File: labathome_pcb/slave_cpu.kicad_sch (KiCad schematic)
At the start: 49 parts, among them J1 HALL, J25 TC-2030, J27 ADDA, J28 Brushless, J34 STM32 EXT, J36 PROG_STM, U16 LM358, U3 DRV8313, U5 STM32G431R8Tx

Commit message: Optimized PCB
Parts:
- removed J25: TC-2030, Connector:Tag-Connect_TC2030-IDC-NL_2x03_P1.27mm_Vertical, symbol Connector:Conn_ARM_SWD_TagConnect_TC2030-NL

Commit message: Bus servos
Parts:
- removed C10, C8, C9: 10p, Capacitor_SMD:C_0402_1005Metric, symbol Device:C
- removed C38: 10n/35V, Capacitor_SMD:C_0402_1005Metric, symbol Device:C
- removed C39: 100u, Capacitor_SMD:CP_Elec_6.3x5.4, symbol Device:C_Polarized
- removed C51: u1/16V, Capacitor_SMD:C_0603_1608Metric, symbol Device:C
- removed C52, C63: u1/35V, Capacitor_SMD:C_0603_1608Metric, symbol Device:C
- removed C61: 4u7/6V3, Capacitor_SMD:C_0402_1005Metric, symbol Device:C
- removed J1: HALL, liebler_CONN:PhoenixContact_MC_1,5_4-G-3.5_1x04_P3.50mm_Horizontal_smallerCourtyard, symbol Connector_Generic:Conn_01x04
- removed J28: Brushless, liebler_CONN:PhoenixContact_MC_1,5_4-G-3.5_1x04_P3.50mm_Horizontal_smallerCourtyard, symbol Connector_Generic:Conn_01x04
- removed R10, R14, R16: 2k2, Resistor_SMD:R_0402_1005Metric, symbol Device:R
- removed R17, R51, R63, R64: 10k, Resistor_SMD:R_0201_0603Metric, symbol Device:R
- removed R38: r1, Resistor_SMD:R_2010_5025Metric, symbol Device:R
- removed U3: DRV8313, Package_SO:HTSSOP-28-1EP_4.4x9.7mm_P0.65mm_EP2.85x5.4mm_ThermalVias, symbol liebler_SEMICONDUCTORS:DRV8313
- added R22: 1k, Resistor_SMD:R_0402_1005Metric, symbol Device:R
- J34: now not fitted
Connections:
- net PB12: no longer U5.34 (PB12)
- net UART3_RX: no longer U5.33 (PB11)
- net UART3_TX: no longer U5.30 (PB10)
- net +24V renamed 5-24V
- net ADC0 renamed ADC0_U1T
- net ADC1 renamed ADC1_U1R
- net Servo0 renamed STEPPER_DIR1
- net Servo1 renamed STEPPER_STEP1
- net Servo2 renamed STEPPER_STEP2
- net Servo3 renamed STEPPER_DIR2
- new net SERVO_BUS_TX_EN: U5.34 (PB12)
- new net STEPPER_UART: R22.2, U5.33 (PB11)
- new net U3T: R22.1, U5.30 (PB10)
- no-connect marks 1 -> 0
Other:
- note added: "T1.1, LPUART1.R"
- note added: "T1.2, LPUART1.T"
- note added: "T1.3"
- note added: "T1.4"
- note added: "T15.1, U2.T"
- note added: "T15.2, U2.R"
- note added: "T2.1"
- note added: "T2.2"
- note removed: "Brushless Driver"
- note removed: "T15.1"
- note removed: "T15.2"

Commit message: Various
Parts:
- added TP2: OP3Q, TestPoint:TestPoint_Pad_1.5x1.5mm, symbol Connector:TestPoint
- added TP3: OP3-, TestPoint:TestPoint_Pad_1.5x1.5mm, symbol Connector:TestPoint
- added TP4: OP3+, TestPoint:TestPoint_Pad_1.5x1.5mm, symbol Connector:TestPoint
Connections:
- net OPAMP3+: now also TP4.1
- net OPAMP3-: now also TP3.1
- net OPAMP3Q: now also TP2.1

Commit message: Merged
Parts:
- removed TP2: OP3Q, TestPoint:TestPoint_Pad_1.5x1.5mm, symbol Connector:TestPoint
- removed TP3: OP3-, TestPoint:TestPoint_Pad_1.5x1.5mm, symbol Connector:TestPoint
- removed TP4: OP3+, TestPoint:TestPoint_Pad_1.5x1.5mm, symbol Connector:TestPoint
- added J26: EXT, Connector_PinHeader_2.54mm:PinHeader_2x03_P2.54mm_Vertical, symbol Connector_Generic:Conn_02x03_Odd_Even
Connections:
- net SERVO_BUS_TX_EN is gone; now on net PB12: U5.34 (PB12)
- net +3V3: now also J26.1 (Pin_1)
- net GND: now also J26.6 (Pin_6)
- net OPAMP3+: now also J26.2 (Pin_2)
- net OPAMP3-: now also J26.3 (Pin_3)
- net OPAMP3Q: now also J26.5 (Pin_5)
- net PB12: now also J26.4 (Pin_4)
- net STEPPER_DIR2 renamed STEPPER_STEP3

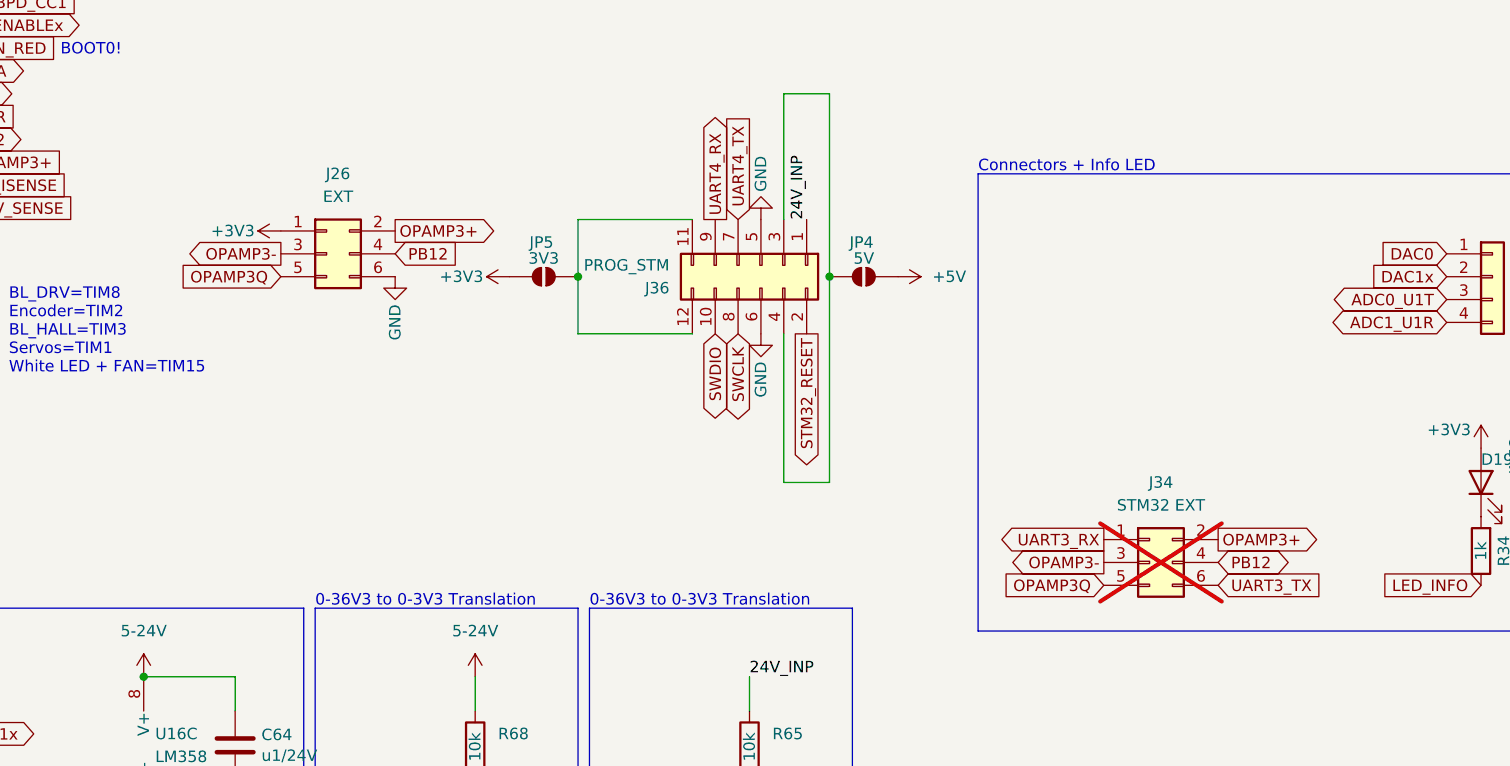
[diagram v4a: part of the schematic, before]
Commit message: Integration of old "webmanager" code (untested)
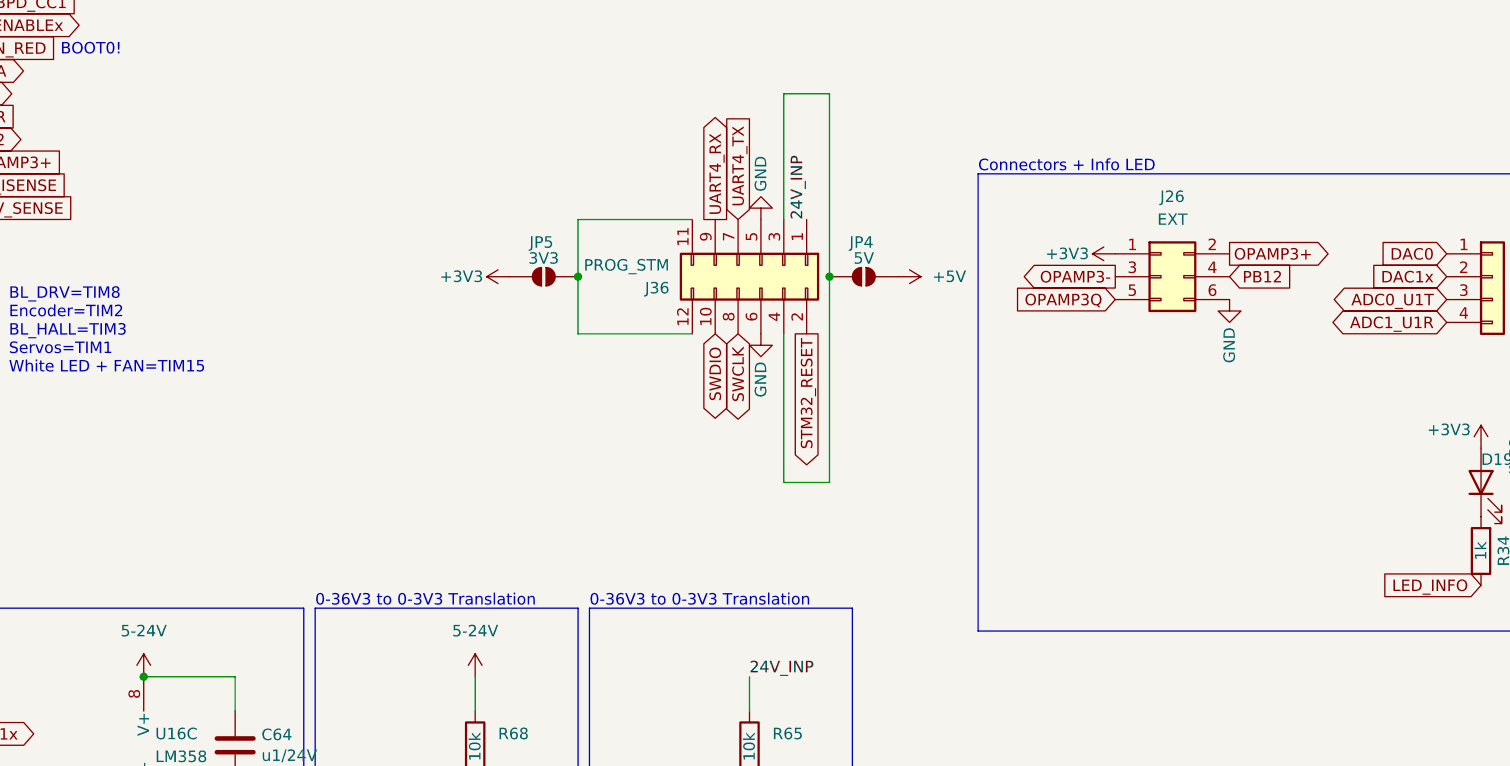
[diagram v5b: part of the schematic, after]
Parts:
- removed J34: STM32 EXT, Connector_PinHeader_2.54mm:PinHeader_2x03_P2.54mm_Vertical, symbol Connector_Generic:Conn_02x03_Odd_Even
- R52: Option Sound only -> (none)
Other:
- moved on the sheet: J26

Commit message: Minor changes
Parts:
- C25, C32, C33, C34, C35, C49, C50: MPN (none) -> GRM033R61A104KE15D; Manufacturer (none) -> Murata Electronics
- C36: MPN (none) -> CL05A475MP5NRNC; Manufacturer (none) -> Samsung Electro-Mechanics
- C37: MPN (none) -> CL05A105KA5NQNC; Manufacturer (none) -> Samsung Electro-Mechanics
- C64: MPN (none) -> CC0603KRX7R9BB104; Manufacturer (none) -> YAGEO
- D19: MPN (none) -> LTST-C230KRKT; Manufacturer (none) -> Lite-On
- FB2: MPN (none) -> BLM18AG601SN1D; Manufacturer (none) -> Murata Electronics
- J26: MPN (none) -> PZ254V-12-6P; Manufacturer (none) -> XFCN
- J27: MPN (none) -> KF2EDGR-3.5-4P; Manufacturer (none) -> Cixi Kefa Elec
- J36: MPN (none) -> PZ254-2-06-S; Manufacturer (none) -> HCTL
- R22, R34, R69, R71: MPN (none) -> 0402WGF1001TCE; Manufacturer (none) -> UNI-ROYAL(Uniroyal Elec)
- R29, R50, R65, R68: MPN (none) -> 0201WMF1002TEE; Manufacturer (none) -> UNI-ROYAL(Uniroyal Elec)
- U16: MPN (none) -> LM358DT; Manufacturer (none) -> STMicroelectronics
- U5: MPN (none) -> STM32G431RBT6; Manufacturer (none) -> STMicroelectronics
